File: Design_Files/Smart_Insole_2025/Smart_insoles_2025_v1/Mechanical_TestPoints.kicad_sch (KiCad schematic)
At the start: 7 parts

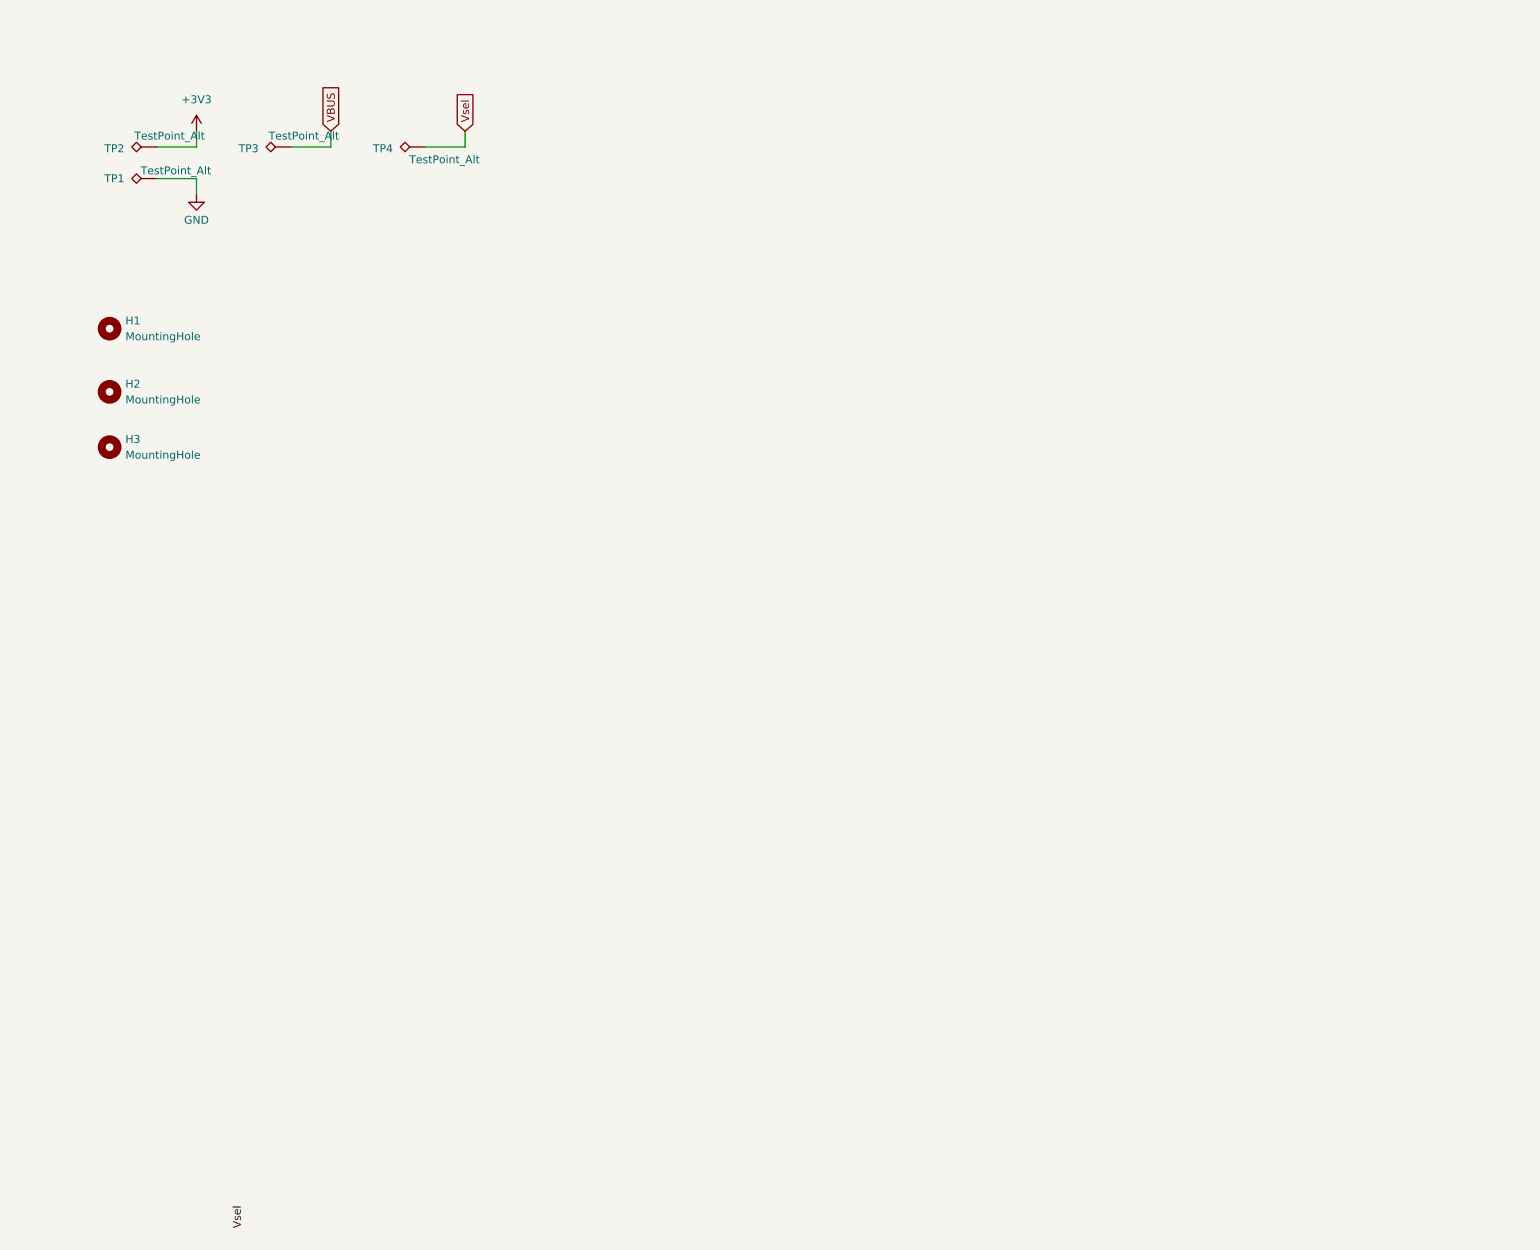
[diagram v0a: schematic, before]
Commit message: SCH: Added test points on idle MCU pins and Power supply. Added ON/OFF switch on VSEL.
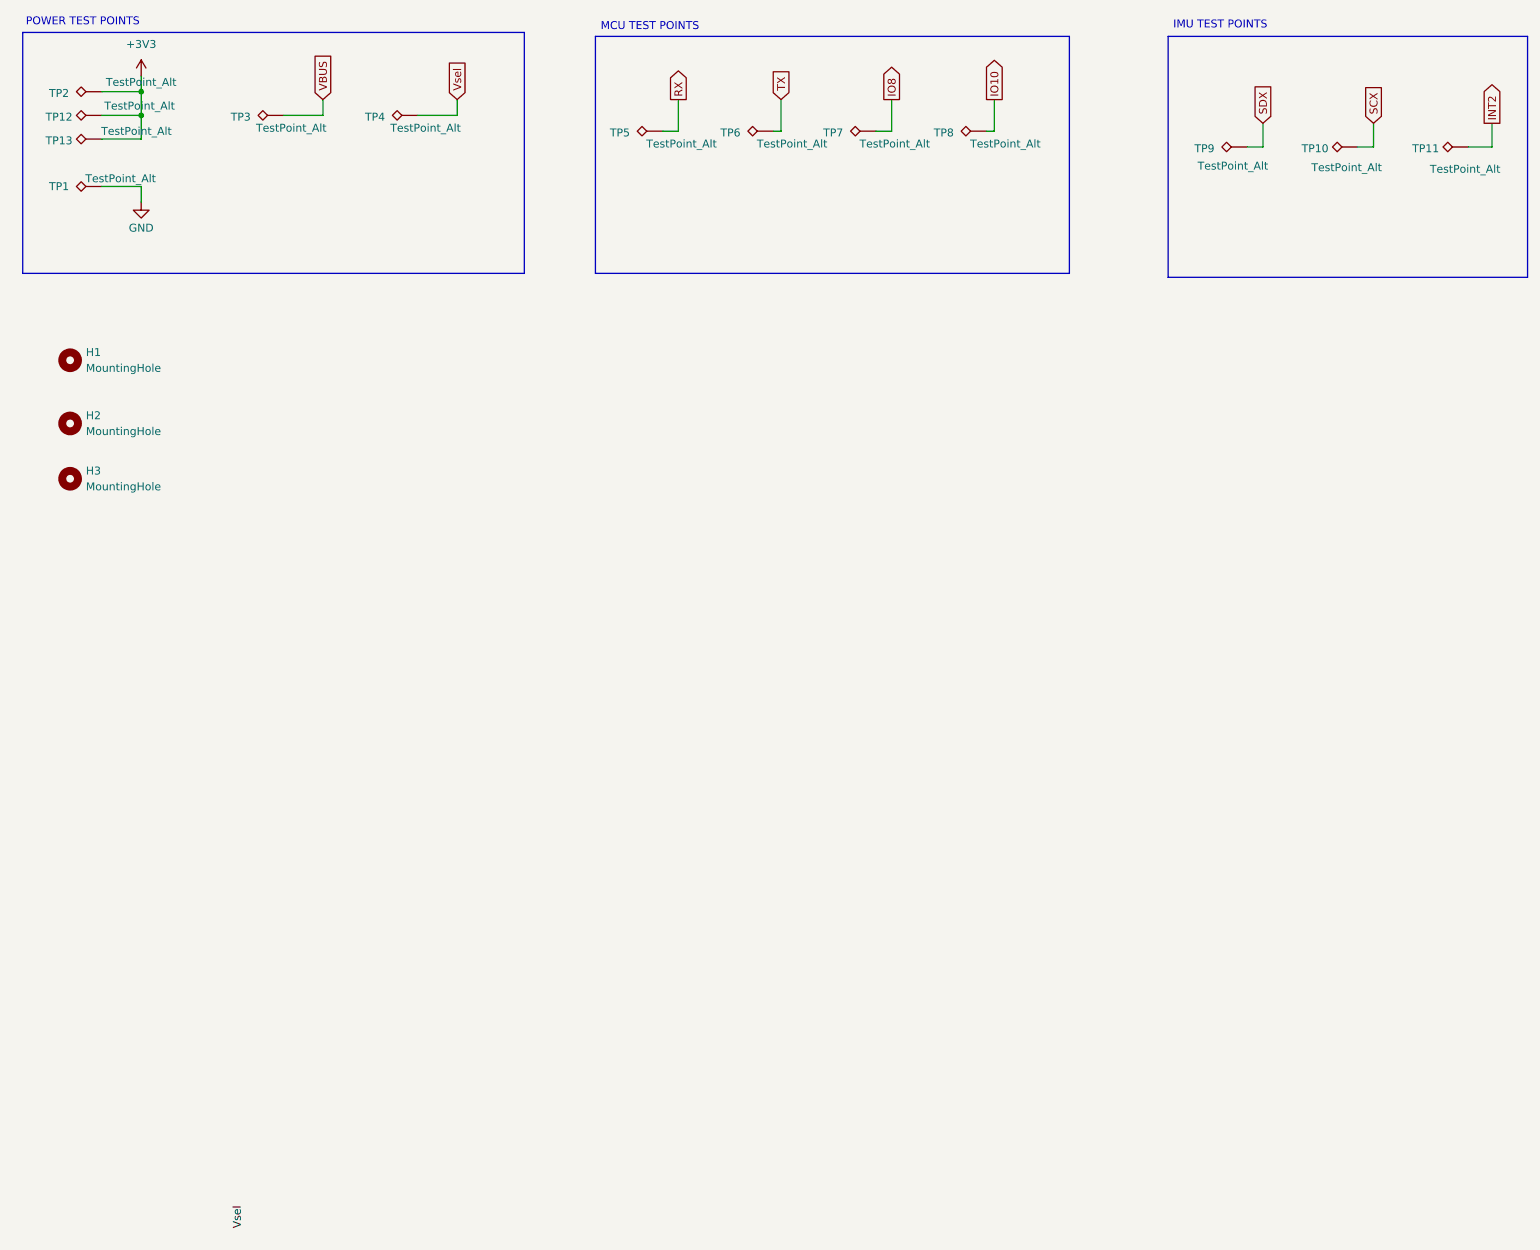
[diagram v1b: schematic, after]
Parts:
- added TP10, TP11, TP12, TP13, TP5, TP6, TP7, TP8, TP9: TestPoint_Alt, TestPoint:TestPoint_Pad_1.0x1.0mm, symbol Connector:TestPoint_Alt
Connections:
- net +3V3: now also TP12.1, TP13.1
- new net INT2: TP11.1
- new net IO10: TP8.1
- new net IO8: TP7.1
- new net RX: TP5.1
- new net SCX: TP10.1
- new net SDX: TP9.1
- new net TX: TP6.1
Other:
- note added: "IMU TEST POINTS"
- note added: "MCU TEST POINTS"
- note added: "POWER TEST POINTS"
- moved on the sheet: H1, H2, H3, TP1, TP2, TP3, TP4

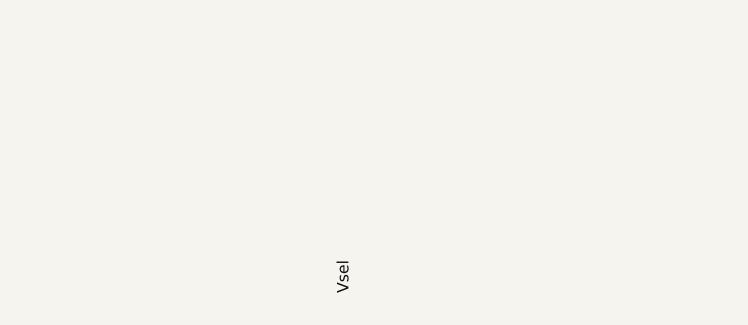
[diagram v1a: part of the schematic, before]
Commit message: PCB: Added 3d models to all components. Also preliminar routing of componentes. Component placemente needs checking.
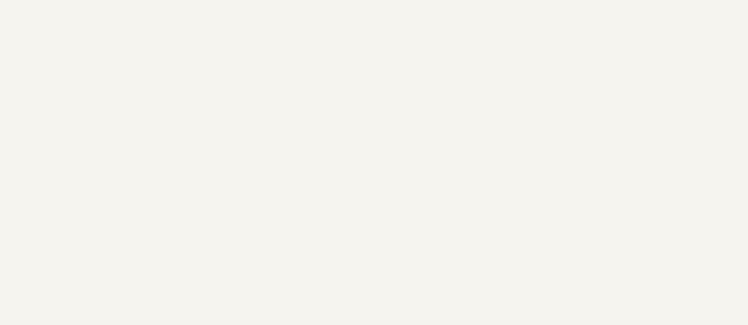
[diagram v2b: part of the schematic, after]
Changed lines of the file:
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@@
-		)
-	)
-	(label "Vsel"
-		(at 54.61 215.9 270)
-		(effects
-			(font
-				(size 1.27 1.27)
-			)
-			(justify right bottom)
 		)
 	)

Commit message: SCH:Added pullup resistors on strapping pins.Added 0.1uF on analog input. Added testpoint on missing pad. PCB:Placed new components.Routing refactoring p1
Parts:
- added TP14: TestPoint_Alt, TestPoint:TestPoint_Pad_1.0x1.0mm, symbol Connector:TestPoint_Alt
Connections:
- new net SDO/SA0: TP14.1
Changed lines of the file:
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@@
+	(wire
+		(pts
+			(xy 218.44 59.69) (xy 219.71 59.69)
+		)
+		(stroke
+			(width 0)
+			(type default)
+		)
+	)
 	(wire
 		(pts
@@
 					(size 1.27 1.27)
 				)
+				(hide yes)
+			)
+		)
+	)
+	(global_label "SDO{slash}SA0"
+		(shape input)
+		(at 219.71 59.69 0)
+		(fields_autoplaced yes)
+		(effects
+			(font
+				(size 1.27 1.27)
+			)
+			(justify left)
+		)
+		(property "Intersheetrefs" "${INTERSHEET_REFS}"
+			(at 231.3433 59.69 0)
+			(effects
+				(font
+					(size 1.27 1.27)
+				)
+				(justify left)
 				(hide yes)
 			)
@@
 					(unit 1)
 				)
+			)
+		)
+	)
+	(symbol
+		(lib_id "Connector:TestPoint_Alt")
+		(at 218.44 59.69 90)
+		(unit 1)
+		(exclude_from_sim no)
+		(in_bom yes)
+		(on_board yes)
+		(dnp no)
+		(property "Reference" "TP14"
+			(at 211.582 59.944 90)
+			(effects
+				(font
+					(size 1.27 1.27)
+				)
+			)
+		)
+		(property "Value" "TestPoint_Alt"
+			(at 217.932 63.246 90)
+			(effects
+				(font
+					(size 1.27 1.27)
+				)
+			)
+		)
+		(property "Footprint" "TestPoint:TestPoint_Pad_1.0x1.0mm"
+			(at 218.44 54.61 0)
+			(effects
+				(font
+					(size 1.27 1.27)
+				)
+				(hide yes)
+			)
+		)
+		(property "Datasheet" "~"
+			(at 218.44 54.61 0)
+			(effects
+				(font
+					(size 1.27 1.27)
+				)
+				(hide yes)
+			)
+		)
+		(property "Description" "test point (alternative shape)"
+			(at 218.44 59.69 0)
+			(effects
+				(font
+					(size 1.27 1.27)
+				)
+				(hide yes)
+			)
+		)
+		(property "MPN" ""
+			(at 218.44 59.69 0)
+			(effects
+				(font
+					(size 1.27 1.27)
+				)
+				(hide yes)
+			)
+		)
+		(property "Manufacturer" ""
+			(at 218.44 59.69 0)
+			(effects
+				(font
+					(size 1.27 1.27)
+				)
+				(hide yes)
+			)
+		)
+		(property "3D Model" ""
+			(at 218.44 59.69 0)
+			(effects
+				(font
+					(size 1.27 1.27)
+				)
+				(hide yes)
+			)
+		)
+		(property "Notes" ""
+			(at 218.44 59.69 0)
+			(effects
+				(font
+					(size 1.27 1.27)
+				)
+				(hide yes)
+			)
+		)
+		(property "LCSC Part #" ""
+			(at 218.44 59.69 0)
+			(effects
+				(font
+					(size 1.27 1.27)
+				)
+				(hide yes)
+			)
+		)
+		(property "LCSC MPN" ""
+			(at 218.44 59.69 0)
+			(effects
+				(font
+					(size 1.27 1.27)
+				)
+				(hide yes)
+			)
+		)
+		(property "LCSC MANUFACTURER" ""
+			(at 218.44 59.69 0)
+			(effects
+				(font
+					(size 1.27 1.27)
+				)
+				(hide yes)
+			)
+		)
+		(pin "1"
+		)
+		(instances
+			(project "Smart_insoles_2025_v1"
+				(path "/f1f3d712-154d-4111-a7c4-f47541abccf8/b19f5448-2243-4e3e-9dc2-3dfe205a5c07"
+					(reference "TP14")
+					(unit 1)
+				)

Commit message: PCB: Added power puddles on Vbat,3v3, VBUS
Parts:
- TP5: footprint TestPoint:TestPoint_Pad_1.0x1.0mm -> TestPoint:TestPoint_Pad_D1.0mm
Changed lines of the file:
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@@
 			)
 		)
-		(property "Footprint" "TestPoint:TestPoint_Pad_1.0x1.0mm"
+		(property "Footprint" "TestPoint:TestPoint_Pad_D1.0mm"
 			(at 121.92 38.1 0)
 			(effects
@@
 			(at 121.92 43.18 0)
 			(effects
+				(font
+					(size 1.27 1.27)
+				)
+				(hide yes)
+			)
+		)
+		(property "Teste Fabricante" ""
+			(at 121.92 43.18 0)
+			(effects
+				(font
+					(size 1.27 1.27)
+				)
+				(hide yes)
+			)
+		)
+		(property "Teste Numero de parte" ""
+			(at 121.92 43.18 0)
+			(effects

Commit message: PCB:Fixed Multiplexer wrong footprint. Flex Connector modified. Fixed DRC Errors and Warnings
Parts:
- TP1, TP10, TP11, TP12, TP13, TP14, TP2, TP3, TP4, TP6, TP7, TP8, TP9: footprint TestPoint:TestPoint_Pad_1.0x1.0mm -> TestPoint:TestPoint_Pad_D1.0mm
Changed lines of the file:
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@@
 					(size 1.27 1.27)
 				)
+				(hide yes)
 			)
 		)
@@
 			)
 		)
-		(property "Footprint" "TestPoint:TestPoint_Pad_1.0x1.0mm"
+		(property "Footprint" "TestPoint:TestPoint_Pad_D1.0mm"
 			(at 215.9 40.64 0)
 			(effects
@@
 					(size 1.27 1.27)
 				)
+				(hide yes)
 			)
 		)
@@
 			)
 		)
-		(property "Footprint" "TestPoint:TestPoint_Pad_1.0x1.0mm"
+		(property "Footprint" "TestPoint:TestPoint_Pad_D1.0mm"
 			(at 173.99 38.1 0)
 			(effects
@@
 					(size 1.27 1.27)
 				)
+				(hide yes)
 			)
 		)
@@
 			)
 		)
-		(property "Footprint" "TestPoint:TestPoint_Pad_1.0x1.0mm"
+		(property "Footprint" "TestPoint:TestPoint_Pad_D1.0mm"
 			(at 82.55 35.56 0)
 			(effects
@@
 					(size 1.27 1.27)
 				)
+				(hide yes)
 			)
 		)
@@
 			)
 		)
-		(property "Footprint" "TestPoint:TestPoint_Pad_1.0x1.0mm"
+		(property "Footprint" "TestPoint:TestPoint_Pad_D1.0mm"
 			(at 139.7 38.1 0)
 			(effects
@@
 					(size 1.27 1.27)
 				)
+				(hide yes)
 			)
 		)
@@
 			)
 		)
-		(property "Footprint" "TestPoint:TestPoint_Pad_1.0x1.0mm"
+		(property "Footprint" "TestPoint:TestPoint_Pad_D1.0mm"
 			(at 31.75 46.99 0)
 			(effects
@@
 					(size 1.27 1.27)
 				)
+				(hide yes)
 			)
 		)
@@
 			)
 		)
-		(property "Footprint" "TestPoint:TestPoint_Pad_1.0x1.0mm"
+		(property "Footprint" "TestPoint:TestPoint_Pad_D1.0mm"
 			(at 31.75 35.56 0)
 			(effects
@@
 					(size 1.27 1.27)
 				)
+				(hide yes)
 			)
 		)
@@
 			)
 		)
-		(property "Footprint" "TestPoint:TestPoint_Pad_1.0x1.0mm"
+		(property "Footprint" "TestPoint:TestPoint_Pad_D1.0mm"
 			(at 60.96 35.56 0)
 			(effects
@@
 					(size 1.27 1.27)
 				)
+				(hide yes)
 			)
 		)
@@
 			)
 		)
-		(property "Footprint" "TestPoint:TestPoint_Pad_1.0x1.0mm"
+		(property "Footprint" "TestPoint:TestPoint_Pad_D1.0mm"
 			(at 233.68 40.64 0)
 			(effects
@@
 					(size 1.27 1.27)
 				)
+				(hide yes)
 			)
 		)
@@
 			)
 		)
-		(property "Footprint" "TestPoint:TestPoint_Pad_1.0x1.0mm"
+		(property "Footprint" "TestPoint:TestPoint_Pad_D1.0mm"
 			(at 31.75 39.37 0)
 			(effects
@@
 					(size 1.27 1.27)
 				)
+				(hide yes)
 			)
 		)
@@
 			)
 		)
-		(property "Footprint" "TestPoint:TestPoint_Pad_1.0x1.0mm"
+		(property "Footprint" "TestPoint:TestPoint_Pad_D1.0mm"
 			(at 156.21 38.1 0)
 			(effects
@@
 					(size 1.27 1.27)
 				)
+				(hide yes)
 			)
 		)
@@
 			)
 		)
-		(property "Footprint" "TestPoint:TestPoint_Pad_1.0x1.0mm"
+		(property "Footprint" "TestPoint:TestPoint_Pad_D1.0mm"
 			(at 31.75 31.75 0)
 			(effects
@@
 					(size 1.27 1.27)
 				)
+				(hide yes)
 			)
 		)
@@
 					(size 1.27 1.27)
 				)
+				(hide yes)
 			)
 		)
@@
 			)
 		)
-		(property "Footprint" "TestPoint:TestPoint_Pad_1.0x1.0mm"
+		(property "Footprint" "TestPoint:TestPoint_Pad_D1.0mm"
 			(at 218.44 54.61 0)
 			(effects
@@
 					(size 1.27 1.27)
 				)
+				(hide yes)
 			)
 		)
@@
 			)
 		)
-		(property "Footprint" "TestPoint:TestPoint_Pad_1.0x1.0mm"
+		(property "Footprint" "TestPoint:TestPoint_Pad_D1.0mm"
 			(at 251.46 40.64 0)
 			(effects

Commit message: PCB: Changed USB position. VERSION SENT TO JLCPCB
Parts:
- added TP15, TP16: TestPoint_Alt, TestPoint:TestPoint_Pad_D1.0mm, symbol Connector:TestPoint_Alt
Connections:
- net GND: now also TP15.1, TP16.1
